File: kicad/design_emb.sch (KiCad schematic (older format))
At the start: 3 parts, among them J1 Conn_01x03, U1 SRX.X.TCT, U2 SRX.X.TCT

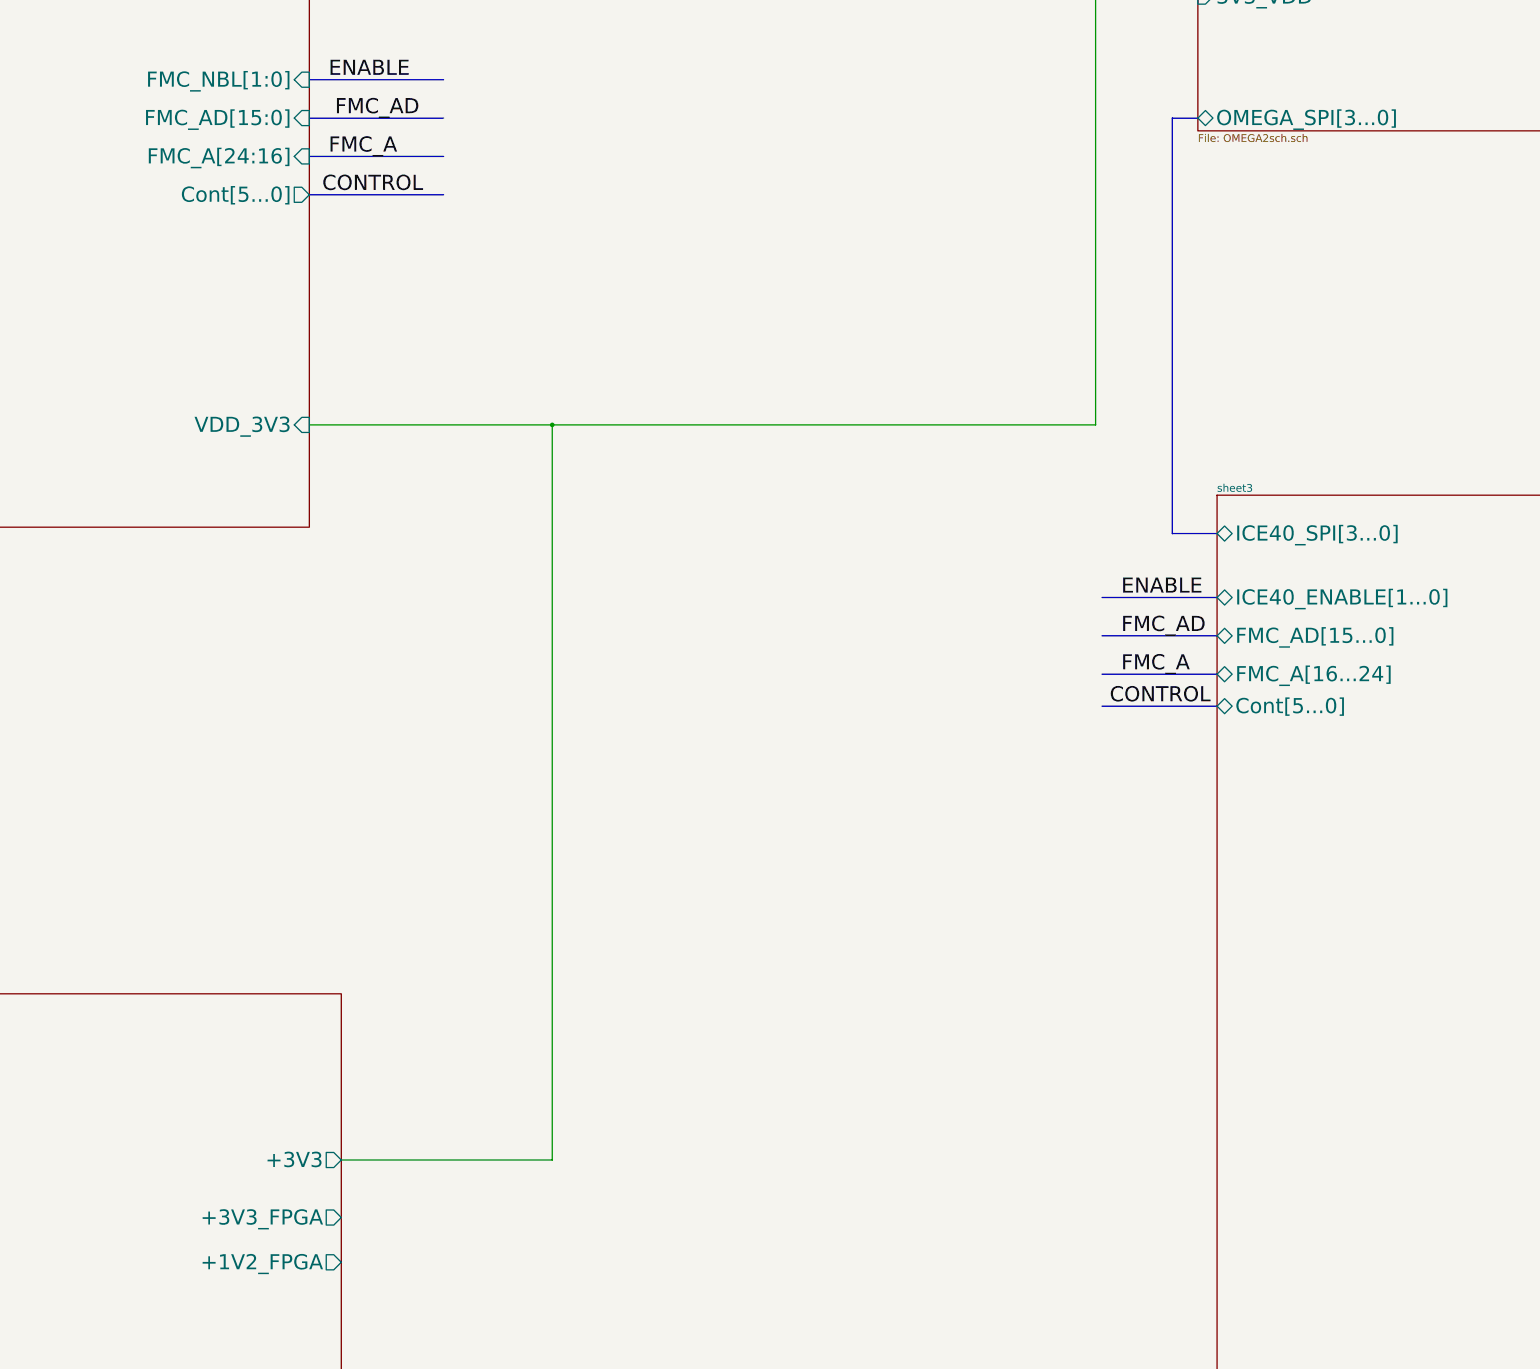
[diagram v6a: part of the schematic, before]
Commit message: buses JTAG, FMC_AD y CTRL
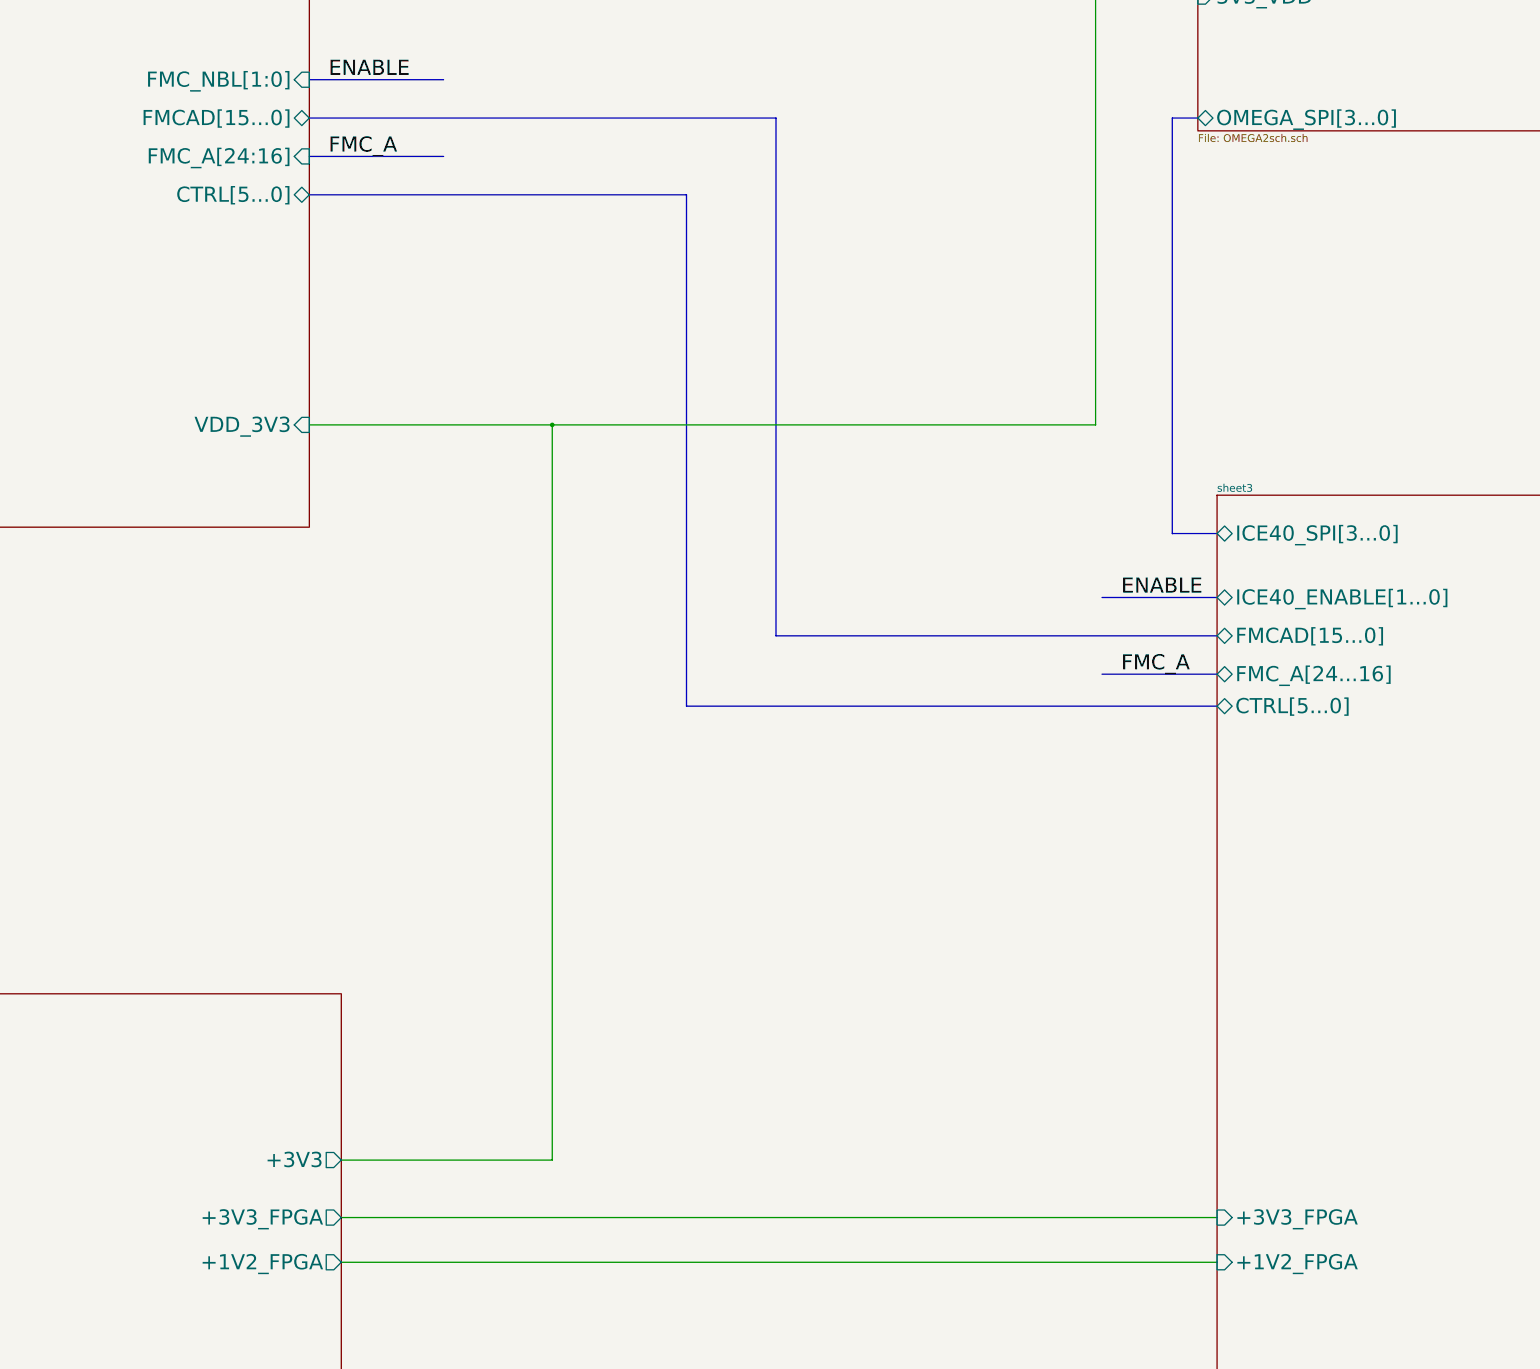
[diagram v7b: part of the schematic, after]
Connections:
- net labels removed: CONTROL, FMC_AD
- wire segments 28 -> 30
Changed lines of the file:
@@
 F0 "Sheet1" 60
 F1 "STM32F446ZETx.sch" 60
-F2 "FMC_AD[15:0]" I R 22950 14100 118
+F2 "FMCAD[15...0]" B R 22950 14100 118
 F3 "FMC_A[24:16]" I R 22950 14400 118
 F4 "FMC_NBL[1:0]" I R 22950 13800 118
@@
 F6 "UART5_TX" O R 22950 7950 118
 F7 "UART5_RX" I R 22950 8150 118
-F8 "Cont[5...0]" O R 22950 14700 118
+F8 "CTRL[5...0]" B R 22950 14700 118
 F9 "BOOT0" I R 22950 8950 118
 F10 "JTAG[5...0]" B R 22950 8700 118
@@
 F0 "sheet3" 60
 F1 "fpga.sch" 60
-F2 "FMC_AD[15...0]" B L 30050 18150 118
-F3 "FMC_A[16...24]" B L 30050 18450 118
+F2 "FMCAD[15...0]" B L 30050 18150 118
+F3 "FMC_A[24...16]" B L 30050 18450 118
 F4 "ICE40_ENABLE[1...0]" B L 30050 17850 118
 F5 "ICE40_SPI[3...0]" B L 30050 17350 118
-F6 "Cont[5...0]" B L 30050 18700 118
+F6 "CTRL[5...0]" B L 30050 18700 118
+F7 "+1V2_FPGA" I L 30050 23050 118
+F8 "+3V3_FPGA" I L 30050 22700 118
 $EndSheet
 $Sheet
@@
 	29100 16500 24850 16500
 Connection ~ 24850 16500
-Text Label 29300 18150 0    118  ~ 0
-FMC_AD
 Text Label 29300 18450 0    118  ~ 0
 FMC_A
-Wire Bus Line
-	22950 14100 24000 14100
-Text Label 23150 14100 0    118  ~ 0
-FMC_AD
 Text Label 23100 14400 0    118  ~ 0
 FMC_A
-Wire Bus Line
-	22950 14700 24000 14700
-Text Label 23050 14700 0    118  ~ 0
-CONTROL
-Text Label 30000 18700 2    118  ~ 0
-CONTROL
 Text Label 29300 17850 0    118  ~ 0
 ENABLE
@@
 	29700 14100 29900 14100
 Wire Bus Line
-	29150 18150 30050 18150
-Wire Bus Line
 	29150 17850 30050 17850
 Wire Bus Line
 	29150 18450 30050 18450
-Wire Bus Line
-	29150 18700 30050 18700
 Wire Bus Line
 	22950 14400 24000 14400
@@
 Wire Wire Line
 	11100 13500 7700 13500
+Wire Wire Line
+	23200 22700 30050 22700
+Wire Wire Line
+	23200 23050 30050 23050
+Wire Bus Line
+	25900 18700 25900 14700
+Wire Bus Line
+	22950 14700 25900 14700
+Wire Bus Line
+	25900 18700 30050 18700
+Wire Bus Line
+	26600 18150 26600 14100
+Wire Bus Line
+	22950 14100 26600 14100
+Wire Bus Line
+	26600 18150 30050 18150
 $EndSCHEMATC

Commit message: design_emb.bak
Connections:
- net labels added: FMCA
- net labels removed: FMC_A
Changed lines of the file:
@@
 EESchema Schematic File Version 4
-LIBS:power
-LIBS:74xx
 LIBS:stm32f446zetx
 LIBS:design_emb-cache
@@
 F1 "STM32F446ZETx.sch" 60
 F2 "FMCAD[15...0]" B R 22950 14100 118
-F3 "FMC_A[24:16]" I R 22950 14400 118
-F4 "FMC_NBL[1:0]" I R 22950 13800 118
-F5 "VDD_3V3" I R 22950 16500 118
+F3 "FMCA[24:16]" B R 22950 14400 118
+F4 "FMCNBL[1:0]" B R 22950 13800 118
+F5 "VDD3V3" I R 22950 16500 118
 F6 "UART5_TX" O R 22950 7950 118
 F7 "UART5_RX" I R 22950 8150 118
@@
 F1 "fpga.sch" 60
 F2 "FMCAD[15...0]" B L 30050 18150 118
-F3 "FMC_A[24...16]" B L 30050 18450 118
-F4 "ICE40_ENABLE[1...0]" B L 30050 17850 118
-F5 "ICE40_SPI[3...0]" B L 30050 17350 118
+F3 "FMCA[24...16]" B L 30050 18450 118
+F4 "ICE40ENABLE[1...0]" B L 30050 17850 118
+F5 "ICE40SPI[3...0]" B L 30050 17350 118
 F6 "CTRL[5...0]" B L 30050 18700 118
 F7 "+1V2_FPGA" I L 30050 23050 118
@@
 F5 "UART_RX" I L 29900 7300 118
 F6 "UART_TX" O L 29900 7550 118
-F7 "OMEGA_SPI[3...0]" B L 29900 14100 118
+F7 "OMEGASPI[3...0]" B L 29900 14100 118
 F8 "JTAG[5...0]" B L 29900 8700 118
 F9 "BOOT0" O L 29900 8950 118
@@
 Connection ~ 24850 16500
 Text Label 29300 18450 0    118  ~ 0
-FMC_A
+FMCA
 Text Label 23100 14400 0    118  ~ 0
-FMC_A
+FMCA
 Text Label 29300 17850 0    118  ~ 0
 ENABLE
